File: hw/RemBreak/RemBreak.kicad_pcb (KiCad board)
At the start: 2 copper layers, 40 x 80 mm, 77 parts, among them IC1 LTC2943IDD#TRPBF, J1 Screw_Terminal_01x04, J2 Screw_Terminal_01x04, J3 Screw_Terminal_01x02, J4 Conn_01x03_MountingPin, J5 Conn_02x06_Odd_Even, J6 Conn_01x07, J7 Conn_01x07, J8 Conn_01x03, Q1 BC337, Q10 BC337, Q11 BC847, Q2 BC847, Q3 BC847, Q4 BC337, Q5 BC337, Q6 SiS415DNT, Q7 BC847, Q8 BC337, Q9 BC847, U1 INA219BxDCN, U2 MAX40200AUK, U3 BD48ExxG, U4 BD48ExxG, U5 L7805, U6 L7805, U7 XC6220B331MR, U8 MAX40200AUK

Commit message: routing in progress
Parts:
- R10, U4: moved to F.Cu
- moved U4 23.7 mm to (146.6, 100.4), turned to 180 degrees
- moved R3 13.5 mm to (135.8, 113.5), turned to -90 degrees
- moved R10 12.3 mm to (133.4, 113.5), turned to 90 degrees
- moved R31 7.60 mm to (142.1, 119.4)
- moved R36 6.00 mm to (149.5, 123.8), turned to 180 degrees
- moved R32 5.35 mm to (142.8, 122.2), turned to -90 degrees
- moved R35 4.72 mm to (144.8, 120.9), turned to -90 degrees
- moved R34 4.66 mm to (132.6, 102.2)
- moved U7 4.63 mm to (135.7, 102.2)
- moved R33 4.37 mm to (140.6, 122.2), turned to -90 degrees
- moved R11 3.83 mm to (135.8, 128.6), turned to -90 degrees
- moved R2 3.72 mm to (154.1, 128.0), turned to 180 degrees
- moved U8 3.36 mm to (145.7, 110.0)
- moved C4 2.72 mm to (142.2, 110.0)
- moved Q9 0.70 mm to (149.7, 120.8)
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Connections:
- J5 pad 3: +3V3 -> /control_connector/ONOFF
- J5 pad 4: +5V -> /control_connector/VBATT
- J5 pad 5: /control_connector/ONOFF -> +5V
- J5 pad 6: /control_connector/VBATT -> +3V3
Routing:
- net /control_connector/LED GREEN: track 11.9 -> 46.4 mm
- net /break_control/VBUS: track 0.00 -> 28.6 mm, vias 0 -> 1
- net /control_connector/ONOFF: track 27.2 -> 55.1 mm, vias 0 -> 1
- net +5V: track 14.3 -> 38.4 mm, vias 1 -> 2
- net /control_connector/LED BLUE: track 19.1 -> 42.7 mm
- net Net-(U3-VOUT): track 26.6 -> 40.1 mm
- net +3V3: track 39.4 -> 47.9 mm
- net /break_control/BALARM: track 35.9 -> 33.0 mm, vias 1 -> 2
- net /control_connector/VBATT: track 37.2 -> 34.6 mm
- net /break_control/I2C.SDA: track 66.3 -> 68.1 mm
- net +7.5V: track 43.9 -> 45.2 mm
- net /break_control/I2C.SCL: track 64.7 -> 65.2 mm

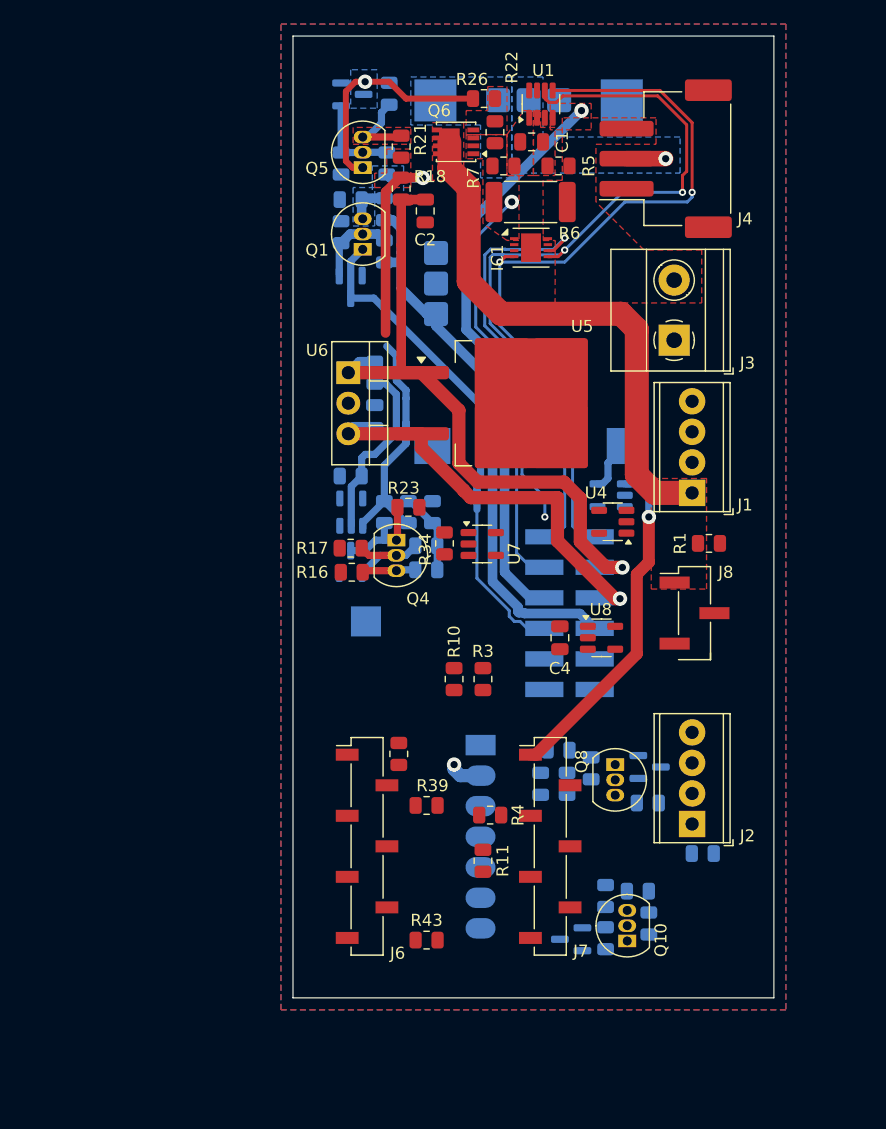
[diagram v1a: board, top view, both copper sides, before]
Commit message: first version of routing finished
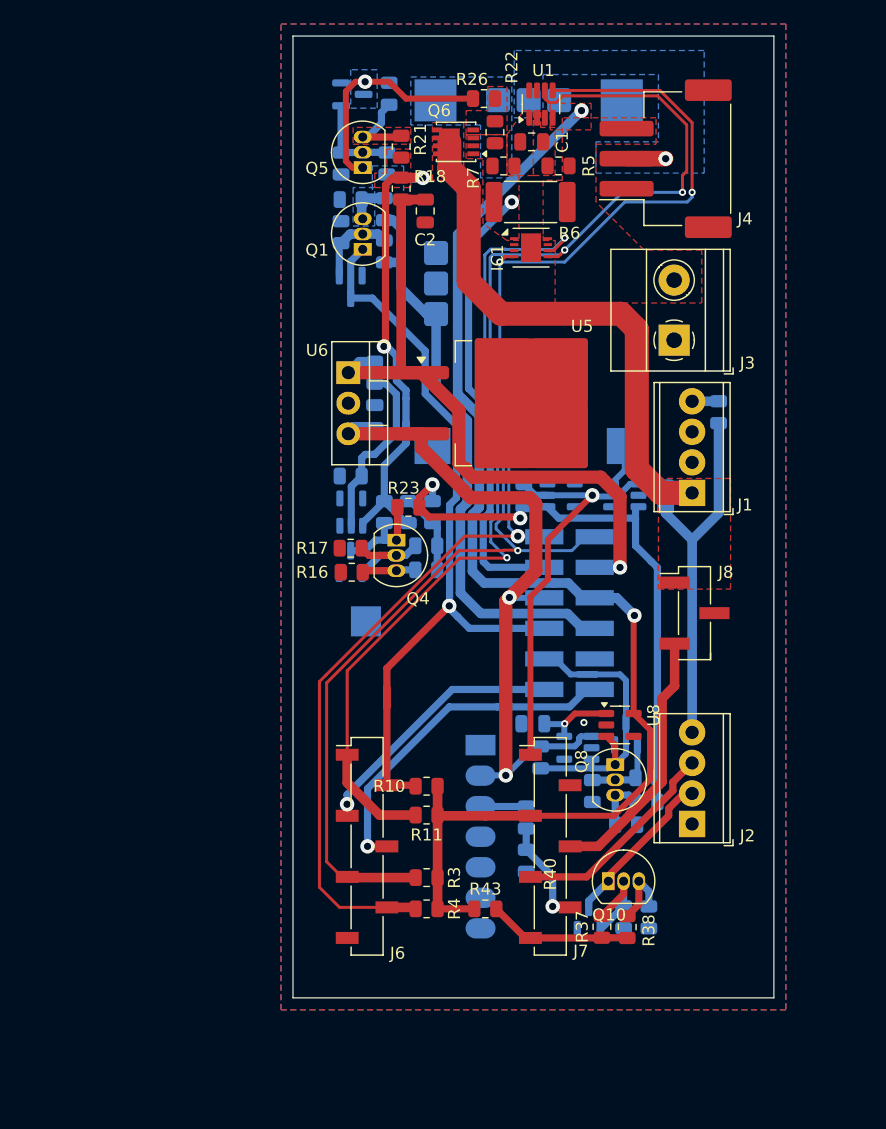
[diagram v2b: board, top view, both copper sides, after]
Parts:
- C4, R1, R34, R39, R40, U4, U7: moved to B.Cu
- R37, R38: moved to F.Cu
- moved R2 36.7 mm to (155.4, 91.3), turned to -90 degrees
- moved R31 21.4 mm to (139.2, 98.2), turned to 90 degrees
- moved R34 19.5 mm to (140.6, 120.0)
- moved U7 18.7 mm to (143.7, 119.2), turned to 180 degrees
- moved R3 17.2 mm to (131.1, 130.0), turned to 180 degrees
- moved R40 13.8 mm to (139.4, 128.6), turned to 90 degrees
- moved R4 9.42 mm to (131.1, 132.6)
- moved R10 9.20 mm to (131.1, 122.4), turned to 180 degrees
- moved R33 8.93 mm to (149.4, 123.7), turned to 180 degrees
- moved R39 8.35 mm to (139.4, 125.0), turned to 90 degrees
- moved C4 7.50 mm to (139.9, 117.2), turned to 180 degrees
- moved U8 7.41 mm to (147.2, 117.3)
- moved R32 6.62 mm to (149.4, 121.7), turned to 180 degrees
- moved R11 6.03 mm to (131.1, 124.8), turned to 180 degrees
- moved R43 5.54 mm to (136.0, 132.6)
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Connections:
- J1 pad 3: Net-(J1-Pin_3) -> GND
- J1 pad 4: GND -> Net-(J1-Pin_4)
- J2 pad 1: Net-(J2-Pin_1) -> GND
- J2 pad 4: GND -> Net-(J2-Pin_4)
- J5 pad 1: /break_control/I2C.SCL -> /break_control/I2C.SDA
- J5 pad 10: /break_control/DISPLAY.DI -> /control_connector/LED RED
- J5 pad 12: GND -> /break_control/DISPLAY.DI
- J5 pad 2: /break_control/I2C.SDA -> /break_control/I2C.SCL
- J5 pad 5: +5V -> +3V3
- J5 pad 6: +3V3 -> +5V
- J5 pad 9: /control_connector/LED RED -> GND
- J6 pad 1: Net-(J6-Pin_1) -> /break_control/BALARM
- J6 pad 2: Net-(J6-Pin_2) -> /control_connector/LED BLUE
- J6 pad 3: /break_control/DISPLAY.DCKI -> /break_control/DISPLAY.DI
- J6 pad 4: /break_control/DISPLAY.DI -> /break_control/DISPLAY.DCKI
- J6 pad 7: /break_control/BUTTON -> unconnected-(J6-Pin_7-Pad7)
- J7 pad 4: BUZZ -> /break_control/SERVO
- J7 pad 5: /control_connector/LED BLUE -> /break_control/BUTTON
- J7 pad 6: /break_control/BALARM -> /break_control/RF SWITCH
- J7 pad 7: unconnected-(J7-Pin_7-Pad7) -> /break_control/BUZZ
- J8 pad 3: Net-(J6-Pin_1) -> /break_control/SERVO
- R1 pad 2: Net-(J2-Pin_1) -> Net-(J2-Pin_4)
- R2 pad 1: Net-(J1-Pin_3) -> Net-(J1-Pin_4)
- R2 pad 2: Net-(J2-Pin_1) -> Net-(J2-Pin_4)
- R37 pad 1: BUZZ -> /break_control/BUZZ
- R38 pad 1: BUZZ -> /break_control/BUZZ
- R39 pad 1: Net-(J6-Pin_2) -> /break_control/RF SWITCH
- R40 pad 2: Net-(J6-Pin_2) -> /break_control/RF SWITCH
- R43 pad 2: /break_control/BUTTON -> /break_control/BUZZ
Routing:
- net +3V3: track 47.9 -> 105.2 mm, vias 1 -> 2
- net /break_control/I2C.SDA: track 68.1 -> 118.0 mm, vias 2 -> 3
- net /power_manager/EN: track 0.00 -> 48.0 mm, vias 0 -> 2
- net /break_control/I2C.SCL: track 65.2 -> 111.5 mm, vias 2 -> 3
- net /break_control/BALARM: track 33.0 -> 68.9 mm
- net Net-(J2-Pin_4): track 0.00 -> 30.3 mm
- net /break_control/DISPLAY.DCKI: track 0.00 -> 28.7 mm, vias 0 -> 1
- net /control_connector/LED RED: track 0.00 -> 26.2 mm
- net /control_connector/LED BLUE: track 42.7 -> 64.9 mm, vias 0 -> 1
- net /break_control/SERVO: track 0.00 -> 21.8 mm
- net /break_control/DISPLAY.DI: track 0.00 -> 21.8 mm, vias 0 -> 1
- net +5V: track 38.4 -> 58.4 mm
- net /break_control/BUTTON: track 0.00 -> 17.8 mm
- net /break_control/BUZZER: track 0.00 -> 13.4 mm
- net /break_control/BUZZ: track 0.00 -> 11.9 mm
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
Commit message: changed board settings and replaced r and c footprints with the ones for handsoldering
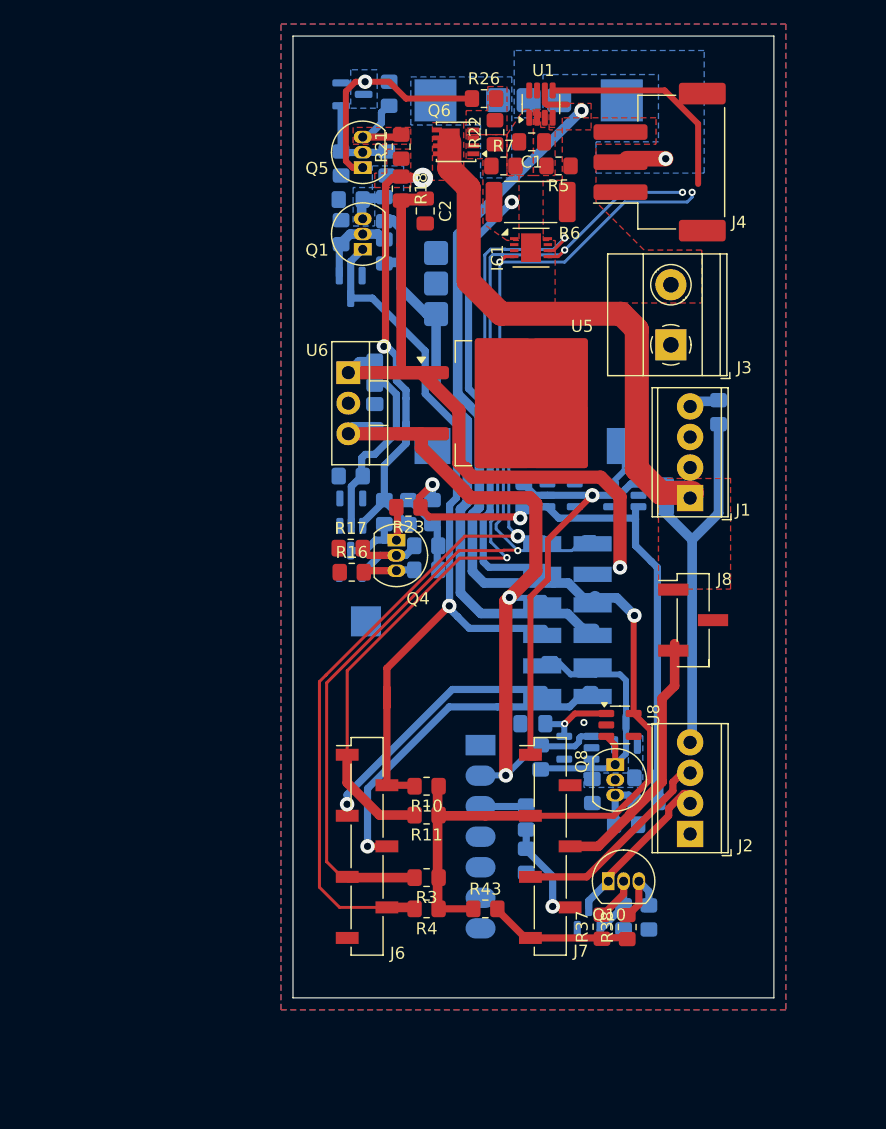
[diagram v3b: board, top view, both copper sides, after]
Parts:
- C1, C2, C3, C4: footprint Capacitor_SMD:C_0805_2012Metric -> Capacitor_SMD:C_0805_2012Metric_Pad1.18x1.45mm_HandSolder
- R1, R10, R11, R12, R13, R14, R15, R16, R17, R18, R19, R2, R20, R21, R22, R23, R24, R25, R26, R27, R28, R29, R3, R30, R31, R32, R33, R34, R35, R36, R37, R38, R39, R4, R40, R41, R42, R43, R5, R7, R8, R9: footprint Resistor_SMD:R_0805_2012Metric -> Resistor_SMD:R_0805_2012Metric_Pad1.20x1.40mm_HandSolder
- moved J2 0.85 mm to (153.0, 126.4)
- moved J5 0.61 mm to (149.2, 108.6)
- moved J8 0.60 mm to (153.3, 108.6)
- moved J4 0.58 mm to (150.5, 70.5)
- moved J3 0.47 mm to (151.4, 85.7)
- moved J1 0.46 mm to (153.0, 98.4)
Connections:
- J5 pad 10: /control_connector/LED RED -> GND
- J5 pad 9: GND -> /control_connector/LED RED
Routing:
- net /break_control/I2C.SDA: track 118.0 -> 99.8 mm
- net Net-(Q8-B): track 6.46 -> 0.02 mm
- added copper zone on B.Cu, net Net-(Q8-B)

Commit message: partially reorganized components and routing
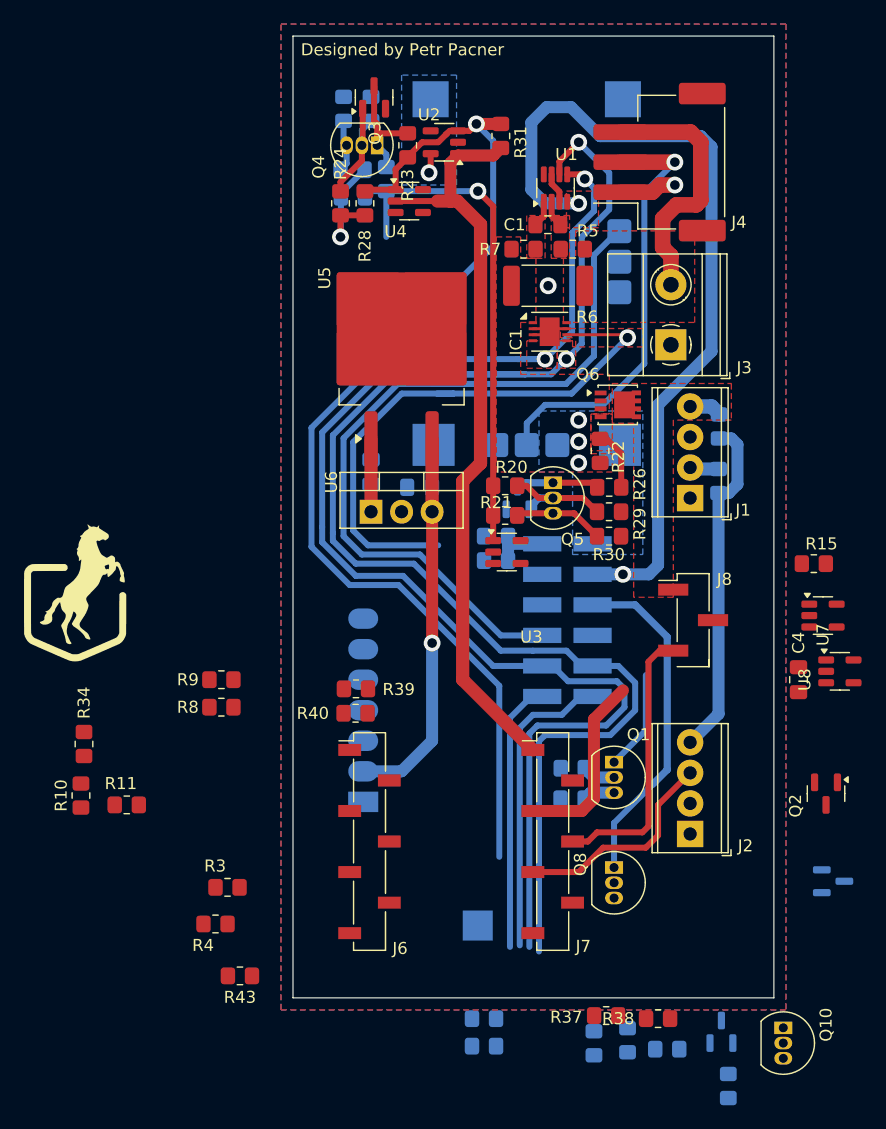
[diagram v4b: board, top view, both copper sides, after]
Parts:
- added REF**: OSHW-Symbol_6.7x6mm_SilkScreen, Symbol:OSHW-Symbol_6.7x6mm_SilkScreen, B.Cu at (109.7, 78.5)
- C2, R16, R17, R18: moved to B.Cu
- C4, Q2, Q3, R15, R20, R24, R28, R29, R30, R31, R34, R39, R40, R8, R9, U2, U3, U4, U7: moved to F.Cu
- moved Q2 57.8 mm to (164.3, 123.0)
- moved R13 53.2 mm to (143.3, 123.4)
- moved R12 48.6 mm to (143.3, 120.9), turned to 0 degrees
- moved Q1 47.5 mm to (146.7, 120.4), turned to -90 degrees
- moved R9 41.4 mm to (114.0, 113.5), turned to 0 degrees
- moved R30 41.1 mm to (146.3, 101.6), turned to 180 degrees
- moved R8 40.3 mm to (114.0, 115.8), turned to 0 degrees
- moved R15 39.2 mm to (163.3, 103.9), turned to 180 degrees
- moved Q3 38.7 mm to (126.7, 65.1)
- moved R16 38.6 mm to (124.2, 66.1), turned to -90 degrees
- moved R34 38.0 mm to (102.6, 118.9)
- moved R17 36.6 mm to (126.5, 66.1), turned to -90 degrees
- moved R29 36.5 mm to (146.3, 99.6), turned to 180 degrees
- moved Q7 36.3 mm to (138.7, 98.4), turned to 90 degrees
- moved R26 34.0 mm to (146.3, 97.5)
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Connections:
- J1 pad 1: +7.5V -> GND
- J1 pad 2: GND -> Net-(J1-Pin_2)
- J1 pad 4: Net-(J1-Pin_4) -> +7.5V
- J2 pad 1: GND -> /break_control/BUZZER
- J2 pad 2: /break_control/BUZZER -> GND
- J5 pad 1: /break_control/I2C.SDA -> /control_connector/VBATT
- J5 pad 10: GND -> /break_control/I2C.SCL
- J5 pad 2: /break_control/I2C.SCL -> /control_connector/ONOFF
- J5 pad 3: /control_connector/ONOFF -> +3V3
- J5 pad 4: /control_connector/VBATT -> +5V
- J5 pad 5: +3V3 -> /control_connector/LED RED
- J5 pad 6: +5V -> GND
- J5 pad 7: /control_connector/LED GREEN -> /control_connector/LED BLUE
- J5 pad 8: /control_connector/LED BLUE -> /control_connector/LED GREEN
- J5 pad 9: /control_connector/LED RED -> /break_control/I2C.SDA
- R2 pad 1: Net-(J1-Pin_4) -> Net-(J1-Pin_2)
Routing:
- net /control_connector/LED BLUE: track 64.9 -> 8.34 mm, vias 1 -> 0
- net +7.5V: track 47.4 -> 2.71 mm
- net /power_manager/EN: track 48.0 -> 91.5 mm, vias 2 -> 1
- net /control_connector/ONOFF: track 53.6 -> 13.3 mm, vias 1 -> 0
- net /control_connector/VBATT: track 37.7 -> 0.00 mm, vias 1 -> 3
- net Net-(J4-Pin_2): track 3.25 -> 36.0 mm
- net /break_control/VBUS: track 34.5 -> 62.5 mm, vias 1 -> 0
- net +5V: track 58.4 -> 33.9 mm, vias 2 -> 1
- net /break_control/I2C.SDA: track 99.8 -> 121.6 mm, vias 3 -> 2
- net Net-(IC1-SENSE-): track 0.00 -> 21.4 mm
- net /break_control/BALARM: track 68.9 -> 47.9 mm, vias 2 -> 1
- net +3V3: track 105.2 -> 84.8 mm
- net /control_connector/LED GREEN: track 48.8 -> 66.6 mm
- net Net-(U3-VDD): track 15.4 -> 0.00 mm
- net /break_control/BUZZER: track 13.4 -> 0.00 mm
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- added copper zone on F.Cu, net /break_control/BALARM
- added copper zone on F.Cu, net /break_control/I2C.SCL
- added copper zone on F.Cu, net /break_control/I2C.SDA
- added copper zone on B.Cu, net Net-(M1-Vin)
- removed copper zone on B.Cu, net Net-(J4-Pin_2)
- removed copper zone on B.Cu, net Net-(Q1-E)
- removed copper zone on B.Cu, net Net-(Q5-C)
- removed copper zone on F.Cu, net Net-(Q5-E)
- removed copper zone on B.Cu, net Net-(Q8-B)
- removed copper zone on B.Cu, net Net-(U3-VOUT)
- removed copper zone on F.Cu, net Net-(U3-VOUT)
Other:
- board text added: "Designed by Petr Pacner"

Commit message: components placed and tracks routed - missing gnd connections and have to refactor the resistors under MCU
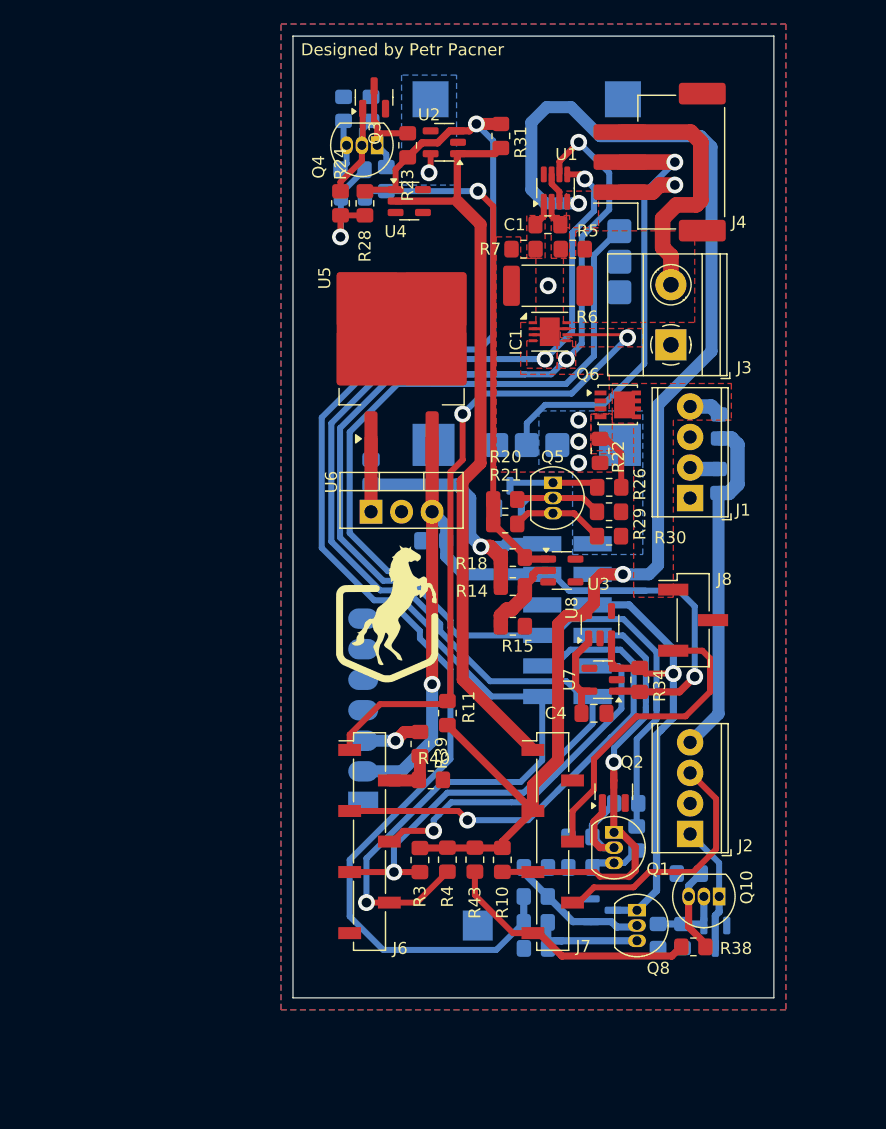
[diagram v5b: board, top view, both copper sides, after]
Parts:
- added REF**: WEEE-Logo_4.2x6mm_SilkScreen, Symbol:WEEE-Logo_4.2x6mm_SilkScreen, B.Cu at (125.5, 89.4)
- R14, R18: moved to F.Cu
- R37, R8, R9: moved to B.Cu
- moved R34 46.5 mm to (148.8, 113.6), turned to -90 degrees
- moved R9 37.0 mm to (148.6, 126.7), turned to -90 degrees
- moved R10 35.5 mm to (137.4, 128.5), turned to -90 degrees
- moved R8 34.6 mm to (147.7, 123.8), turned to 180 degrees
- moved R11 27.7 mm to (132.8, 116.3), turned to 90 degrees
- moved R15 25.6 mm to (138.3, 109.1)
- moved R43 21.8 mm to (135.1, 128.5), turned to -90 degrees
- moved U8 20.3 mm to (145.5, 109.0), turned to 90 degrees
- moved R4 20.0 mm to (132.8, 128.5), turned to -90 degrees
- moved Q9 19.4 mm to (145.7, 132.7)
- moved U7 19.1 mm to (145.8, 113.5), turned to 180 degrees
- moved Q2 17.7 mm to (146.7, 122.9), turned to 90 degrees
- moved C4 17.2 mm to (145.0, 116.3), turned to 0 degrees
- moved R35 16.3 mm to (140.2, 129.2), turned to 180 degrees
- moved R3 16.2 mm to (130.6, 128.5), turned to -90 degrees
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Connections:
- J5 pad 10: /break_control/I2C.SCL -> /break_control/DISPLAY.DI
- J5 pad 11: /break_control/DISPLAY.DCKI -> /break_control/I2C.SDA
- J5 pad 12: /break_control/DISPLAY.DI -> /break_control/I2C.SCL
- J5 pad 9: /break_control/I2C.SDA -> /break_control/DISPLAY.DCKI
- J6 pad 2: /control_connector/LED BLUE -> /break_control/RF SWITCH
- J7 pad 5: /break_control/BUTTON -> /control_connector/LED BLUE
- J7 pad 6: /break_control/RF SWITCH -> /break_control/BUTTON
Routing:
- net +5V: track 33.9 -> 77.7 mm, vias 1 -> 2
- net /power_manager/EN: track 91.5 -> 123.4 mm
- net +3V3: track 84.8 -> 114.9 mm
- net /control_connector/LED BLUE: track 8.34 -> 36.8 mm, vias 0 -> 1
- net /control_connector/LED GREEN: track 66.6 -> 93.5 mm
- net /break_control/DISPLAY.DI: track 22.5 -> 46.9 mm, vias 0 -> 1
- net /break_control/BUZZ: track 0.00 -> 21.5 mm
- net /control_connector/ONOFF: track 13.3 -> 31.1 mm, vias 0 -> 1
- net /control_connector/LED RED: track 28.3 -> 40.8 mm, vias 0 -> 1
- net Net-(Q8-B): track 0.00 -> 11.8 mm
- net /break_control/BUZZER: track 0.00 -> 10.7 mm
- net Net-(Q8-E): track 0.00 -> 10.2 mm
- net /break_control/BALARM: track 47.9 -> 56.3 mm, vias 1 -> 2
- net Net-(Q1-B): track 2.75 -> 11.1 mm
- net Net-(U7-VOUT): track 0.00 -> 7.58 mm
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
